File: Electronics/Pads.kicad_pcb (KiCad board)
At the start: 2 copper layers, 7 parts, among them P1 Header, P2 CONN_01X02, SW1 SW_PUSH, SW2 SW_PUSH, SW3 SW_PUSH, SW4 SW_PUSH, SW5 ALPS_SKQUAAA010

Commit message: Created pcb layout V0.1
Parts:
- P1: value Header -> CONN_02X05; footprint Socket_Strips:Socket_Strip_Straight_1x10 -> Socket_Strips:Socket_Strip_Straight_2x05
- moved SW3 50.1 mm to (116.3, 132.1)
- moved SW5 50.1 mm to (105.4, 105.6)
- moved P2 50.1 mm to (109.7, 100.8)
- moved SW1 50.1 mm to (107.4, 123.7)
- moved SW2 50.1 mm to (98.6, 132.1)
- moved SW4 50.1 mm to (107.4, 140.5)
- moved P1 47.6 mm to (124.3, 105.5)
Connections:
- SW4 pad 2: Net-(SW4-Pad2) -> GND
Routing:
- net Net-(P1-Pad5): track 18.3 -> 37.8 mm, vias 0 -> 1
- net Net-(P1-Pad3): track 6.40 -> 24.7 mm, vias 0 -> 1
- net Net-(P1-Pad7): track 27.7 -> 41.8 mm
- net Net-(P1-Pad8): track 14.0 -> 22.4 mm
- net Net-(P1-Pad9): track 27.1 -> 33.5 mm, vias 0 -> 1
- net Net-(P1-Pad10): track 8.67 -> 13.2 mm
- net Net-(P1-Pad4): track 20.5 -> 23.5 mm
- net Net-(P1-Pad6): track 23.9 -> 25.8 mm, vias 1 -> 0
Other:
- board outline added: 34 x 51 mm
- net class Default: clearance 0.2 -> 0.254; trace_width 0.25 -> 0.635; via_dia 0.6 -> 0.508; via_drill 0.4 -> 0.381
- rule trace_clearance: 0.2 -> 0.254

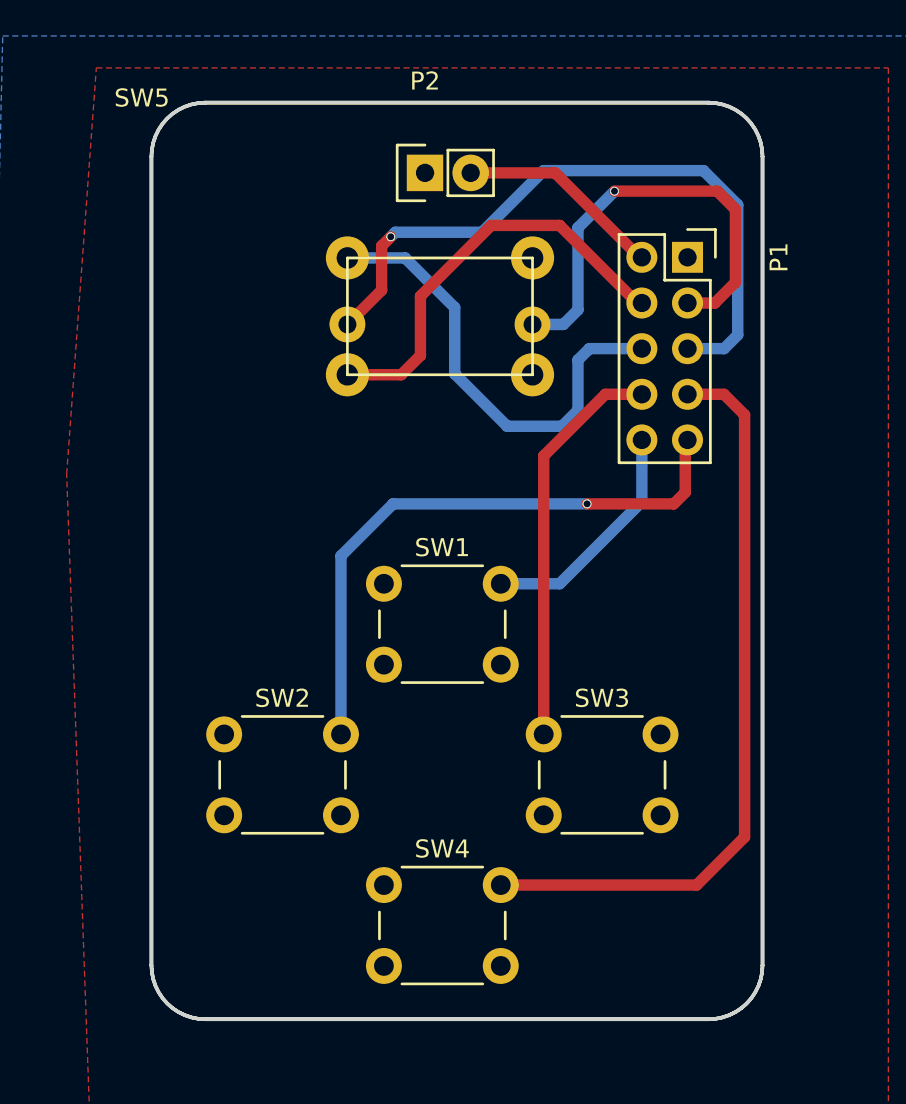
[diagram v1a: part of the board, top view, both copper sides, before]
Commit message: Created pcb, footprints and added logos
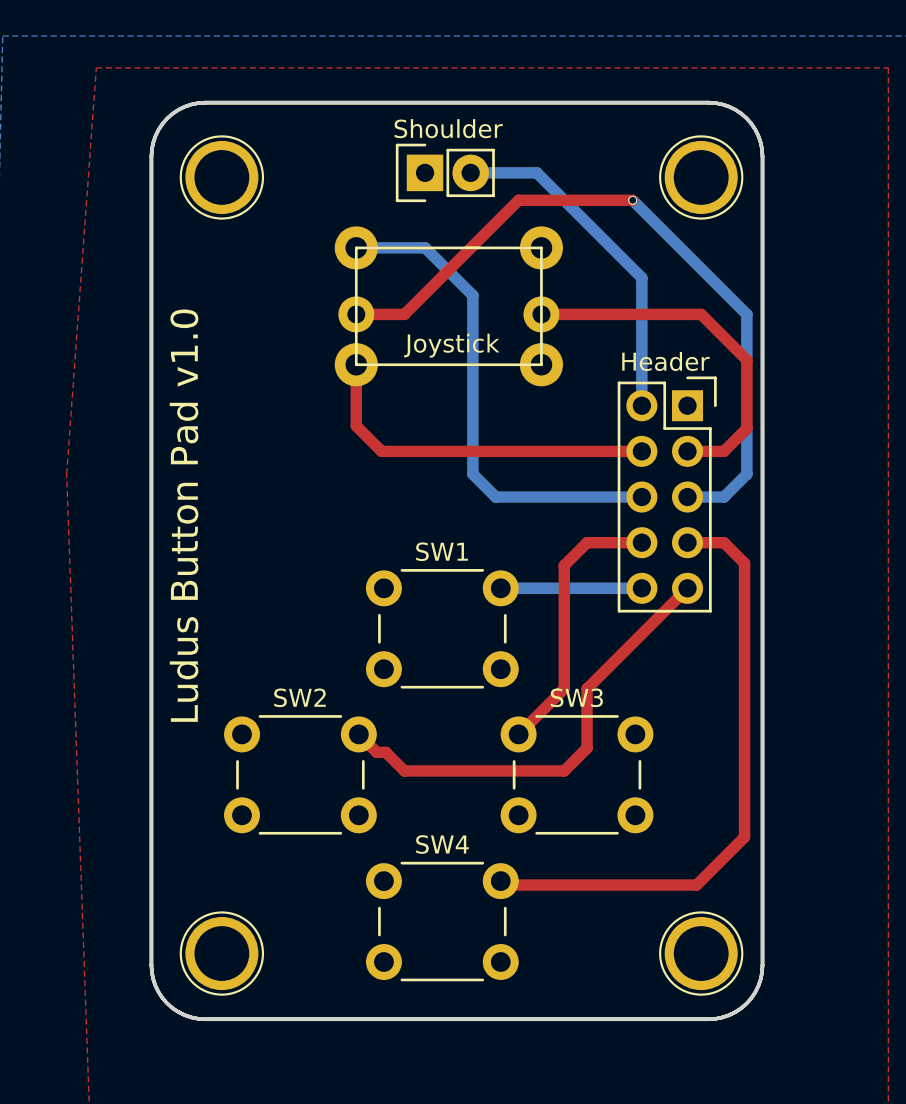
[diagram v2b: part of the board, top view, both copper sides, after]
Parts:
- added ?: , Connect:1pin, F.Cu at (125.1, 144.3)
- added ?: , Connect:1pin, F.Cu at (98.4, 144.3)
- added ?: 1pin, Connect:1pin, F.Cu at (125.1, 101.1)
- added ?: 1pin, Connect:1pin, F.Cu at (98.4, 101.1)
- added G***: LOGO, footprints:ludus, B.Cu at (100.9, 119.9)
- added REF***: OSHW-Logo2_7.3x6mm_SilkScreen, Symbols:OSHW-Logo2_7.3x6mm_SilkScreen, B.Cu at (98.9, 109.3)
- Header: renamed from P1; value CONN_02X05 -> (none)
- Joystick: renamed from SW5; value ALPS_SKQUAAA010 -> joystick
- SW1: value SW_PUSH -> btn1
- SW2: value SW_PUSH -> btn2
- SW3: value SW_PUSH -> btn3
- SW4: value SW_PUSH -> btn4
- Shoulder: renamed from P2; value CONN_01X02 -> Shoulder
- moved Header 8.25 mm to (124.3, 113.8)
- moved SW3 1.40 mm to (114.9, 132.1)
- moved SW2 0.99 mm to (99.5, 132.1)
- moved Joystick 0.75 mm to (105.9, 105.0)
- moved SW1 0.25 mm to (107.4, 124.0)
- moved SW4 0.22 mm to (107.4, 140.2)
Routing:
- net Net-(P1-Pad7): track 41.8 -> 33.6 mm
- net Net-(P1-Pad9): track 33.5 -> 25.3 mm, vias 1 -> 0
- net Net-(P1-Pad2): track 11.5 -> 19.1 mm
- net Net-(P1-Pad8): track 22.4 -> 15.3 mm
- net Net-(P1-Pad10): track 13.2 -> 7.85 mm
- net Net-(P1-Pad3): track 24.7 -> 20.1 mm, vias 1 -> 0
- net Net-(P1-Pad4): track 23.5 -> 19.9 mm
- net Net-(P1-Pad5): track 37.8 -> 39.7 mm
- net Net-(P1-Pad6): track 25.8 -> 27.5 mm
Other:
- board text added: "Ludus Button Pad v1.0"
